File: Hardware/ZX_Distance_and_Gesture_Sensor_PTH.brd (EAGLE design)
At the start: 55.9 x 12.7 mm, 49 parts, among them Q1 MMBT2222A, Q2 MOSFET-NCHANNEL2N7002PW, U1 PIC16F1823-14PINTSSOP, U2 MCP6021T-E/OT, U3 DMC2700UDM, U4 DMC2700UDM, U5 BRM-2A18VERT, U6 TSOP57238TT1

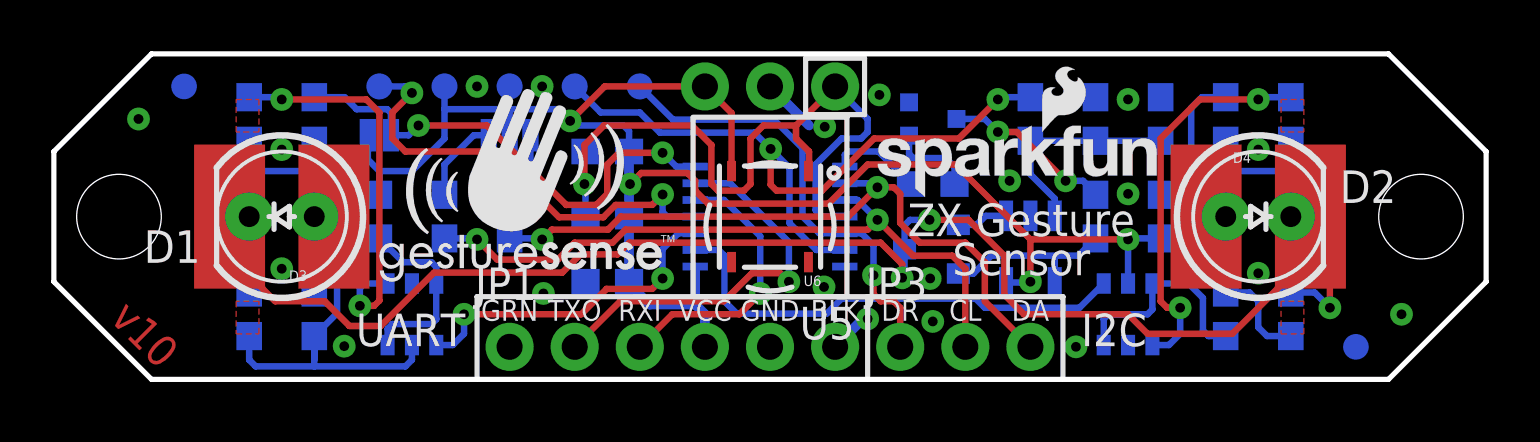
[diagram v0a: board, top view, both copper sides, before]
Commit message: Updated GestureSense Logo
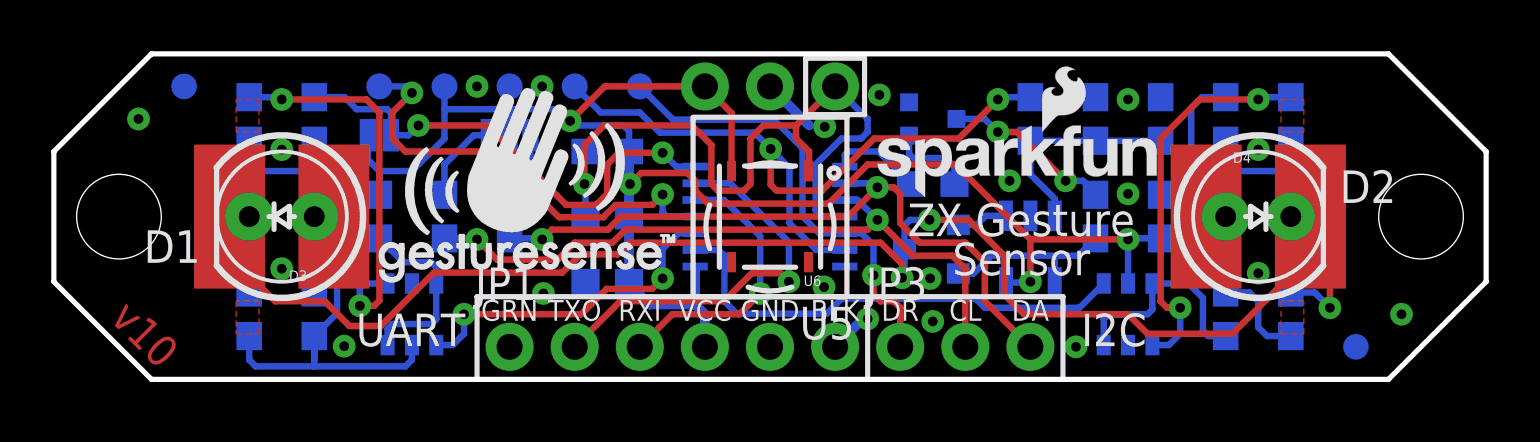
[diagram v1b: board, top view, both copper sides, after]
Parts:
- FRAME1: value (none) -> FRAME-LETTER
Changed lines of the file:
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@@
 <layer number="2" name="Route2" color="1" fill="3" visible="no" active="yes"/>
 <layer number="15" name="Route15" color="4" fill="6" visible="no" active="yes"/>
-<layer number="16" name="Bottom" color="1" fill="1" visible="no" active="yes"/>
+<layer number="16" name="Bottom" color="1" fill="1" visible="yes" active="yes"/>
 <layer number="17" name="Pads" color="2" fill="1" visible="yes" active="yes"/>
 <layer number="18" name="Vias" color="2" fill="1" visible="yes" active="yes"/>
@@
 <layer number="20" name="Dimension" color="15" fill="1" visible="yes" active="yes"/>
 <layer number="21" name="tPlace" color="16" fill="1" visible="yes" active="yes"/>
-<layer number="22" name="bPlace" color="14" fill="1" visible="no" active="yes"/>
+<layer number="22" name="bPlace" color="14" fill="1" visible="yes" active="yes"/>
 <layer number="23" name="tOrigins" color="15" fill="1" visible="yes" active="yes"/>
-<layer number="24" name="bOrigins" color="15" fill="1" visible="no" active="yes"/>
+<layer number="24" name="bOrigins" color="15" fill="1" visible="yes" active="yes"/>
 <layer number="25" name="tNames" color="7" fill="1" visible="no" active="yes"/>
 <layer number="26" name="bNames" color="7" fill="1" visible="no" active="yes"/>
@@
 <layer number="43" name="vRestrict" color="2" fill="10" visible="no" active="yes"/>
 <layer number="44" name="Drills" color="7" fill="1" visible="no" active="yes"/>
-<layer number="45" name="Holes" color="7" fill="1" visible="no" active="yes"/>
+<layer number="45" name="Holes" color="7" fill="1" visible="yes" active="yes"/>
 <layer number="46" name="Milling" color="3" fill="1" visible="no" active="yes"/>
-<layer number="47" name="Measures" color="7" fill="1" visible="no" active="yes"/>
-<layer number="51" name="tDocu" color="6" fill="1" visible="no" active="yes"/>
+<layer number="47" name="Measures" color="7" fill="1" visible="yes" active="yes"/>
+<layer number="51" name="tDocu" color="6" fill="1" visible="yes" active="yes"/>
 <layer number="52" name="bDocu" color="7" fill="1" visible="no" active="yes"/>
 <layer number="3" name="Route3" color="4" fill="3" visible="no" active="no"/>
@@
 <layer number="127" name="_tValues" color="7" fill="1" visible="no" active="no"/>
 <layer number="128" name="_bValues" color="7" fill="1" visible="no" active="no"/>
-<layer number="129" name="Mask" color="7" fill="1" visible="no" active="yes"/>
+<layer number="129" name="Mask" color="7" fill="1" visible="no" active="no"/>
 <layer number="131" name="tAdjust" color="7" fill="1" visible="no" active="no"/>
 <layer number="132" name="bAdjust" color="7" fill="1" visible="no" active="no"/>
@@
 <layer number="223" name="223bmp" color="24" fill="1" visible="no" active="no"/>
 <layer number="224" name="224bmp" color="25" fill="1" visible="no" active="no"/>
-<layer number="225" name="225bmp" color="7" fill="1" visible="no" active="yes"/>
-<layer number="226" name="226bmp" color="7" fill="1" visible="no" active="yes"/>
-<layer number="227" name="227bmp" color="7" fill="1" visible="no" active="yes"/>
-<layer number="228" name="228bmp" color="7" fill="1" visible="no" active="yes"/>
-<layer number="229" name="229bmp" color="7" fill="1" visible="no" active="yes"/>
-<layer number="230" name="230bmp" color="7" fill="1" visible="no" active="yes"/>
-<layer number="231" name="231bmp" color="7" fill="1" visible="no" active="yes"/>
+<layer number="225" name="225bmp" color="7" fill="1" visible="no" active="no"/>
+<layer number="226" name="226bmp" color="7" fill="1" visible="no" active="no"/>
+<layer number="227" name="227bmp" color="7" fill="1" visible="no" active="no"/>
+<layer number="228" name="228bmp" color="7" fill="1" visible="no" active="no"/>
+<layer number="229" name="229bmp" color="7" fill="1" visible="no" active="no"/>
+<layer number="230" name="230bmp" color="7" fill="1" visible="no" active="no"/>
+<layer number="231" name="231bmp" color="7" fill="1" visible="no" active="no"/>
 <layer number="248" name="Housing" color="7" fill="1" visible="no" active="no"/>
 <layer number="249" name="Edge" color="7" fill="1" visible="no" active="no"/>
@@
 </autorouter>
 <elements>
-<element name="FRAME1" library="SparkFun-Aesthetics" package="CREATIVE_COMMONS" value="" x="-25.4" y="-17.78">
-<attribute name="VERSION" value="v10" x="-25.4" y="-17.78" size="1.778" layer="27" display="off"/>
-<attribute name="DESIGNER" value="Shawn Hymel" x="-25.4" y="-17.78" size="1.778" layer="27" display="off"/>
-</element>
+<element name="FRAME1" library="SparkFun-Aesthetics" package="CREATIVE_COMMONS" value="FRAME-LETTER" x="-25.4" y="-17.78"/>
 <element name="U1" library="SparkFun-DigitalIC" package="TSSOP14" value="PIC16F1823-14PINTSSOP" x="0" y="0" rot="MR90">
 <attribute name="PROD_ID" value="IC-11992" x="-3.81" y="17.78" size="1.778" layer="28" rot="MR90" display="off"/>
